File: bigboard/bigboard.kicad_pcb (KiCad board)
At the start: 2 copper layers, 99.1 x 48.3 mm, 69 parts, among them J1 motorA, J2 motorB, J3 USB_B_Mini, J4 device2, J5 device1, J6 battery, Q1 BC547, Q2 BC547, Q3 BC547, Q4 BC547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

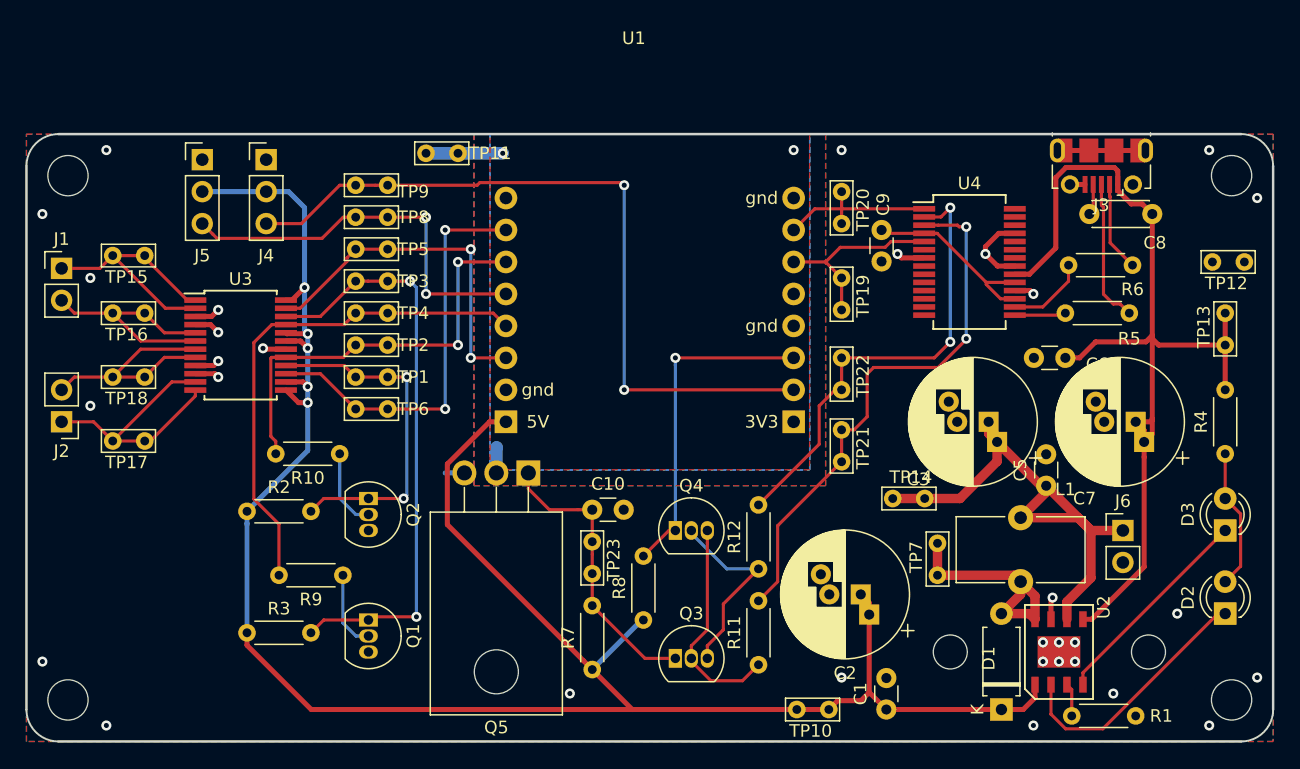
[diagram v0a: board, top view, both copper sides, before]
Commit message: Fix Footprints for kicad 5.1.8
thanks to tobi for the tip how to install a newer
kicad on debian: there is a newer version in
debian-packports.

fixed the libraries and footprints, and changed
the path to relative ones.
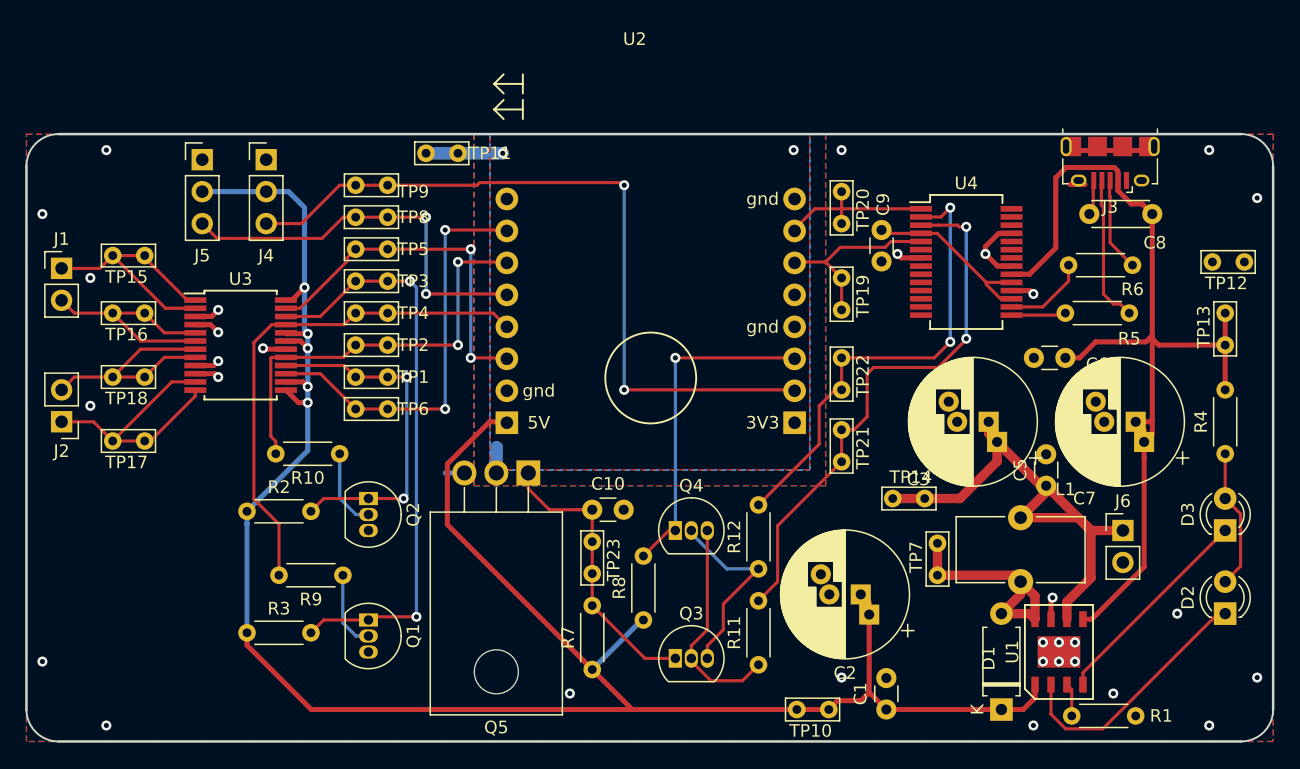
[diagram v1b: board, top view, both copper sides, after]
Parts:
- removed REF** (x4): M3, MountingHole:MountingHole_3.2mm_M3
- removed REF** (x2): M2.5, MountingHole:MountingHole_2.7mm_M2.5
- J3: footprint Connector_USB:USB_Micro-B_Molex-105017-0001 -> Connector_USB:USB_Micro-B_Amphenol_10118194_Horizontal
- U1: value ESPCAM -> TP5400; footprint espcam:ESPCAM_bottom -> TP5400:ESOP8-F.Cu-only
- U2: value TP5400 -> ESPCAM; footprint TP5400:ESOP8-F.Cu-only -> espcam:ESPCAM_bottom
- moved U1 51.3 mm to (197.6, 119.9)
- moved U2 51.2 mm to (163.9, 81.4)
- moved J3 0.74 mm to (201.7, 81.0)
- moved U4 0.25 mm to (190.2, 88.9)
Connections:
- U1 pad 1: (no net) -> vout
- U1 pad 2: pwmb -> LEDchrg
- U1 pad 3: bin1 -> Net-(R1-Pad1)
- U1 pad 4: gpio15 -> LEDstdby
- U1 pad 5: ain1 -> vcc
- U1 pad 6: pwma -> bat
- U1 pad 7: espGND -> GND
- U1 pad 8: vout -> lx
- U1 pad 9: espGND -> GND
- U2 pad 1: vout -> (no net)
- U2 pad 2: LEDchrg -> pwmb
- U2 pad 3: Net-(R1-Pad1) -> bin1
- U2 pad 4: LEDstdby -> gpio15
- U2 pad 5: vcc -> ain1
- U2 pad 6: bat -> pwma
- U2 pad 7: GND -> espGND
- U2 pad 8: lx -> vout
- U2 pad 9: GND -> espGND
